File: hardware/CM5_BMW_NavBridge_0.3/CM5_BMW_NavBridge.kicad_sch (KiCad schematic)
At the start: 19 parts, among them CN1 10164227-1001A1RLF, CN2 10164227-1001A1RLF, CN3 X1313 Car connector, CN4 Molex to X1313 NAV connector, J1 Conn_01x04, SW1 SW_nRPIBOOT, SW2 SW_DIP_x02

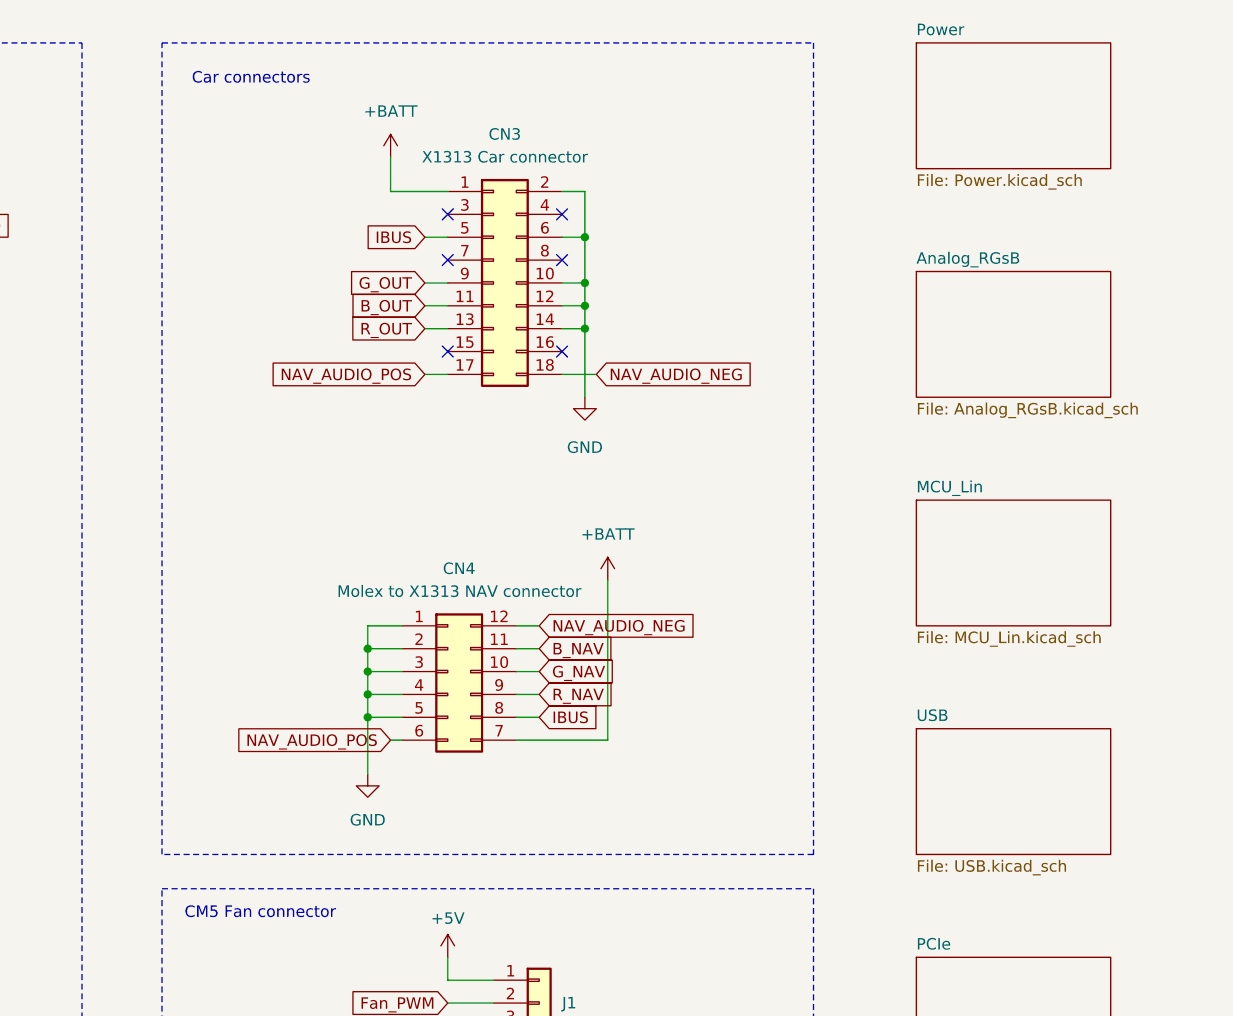
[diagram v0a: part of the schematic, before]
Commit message: finalized deletions and updated net deletes
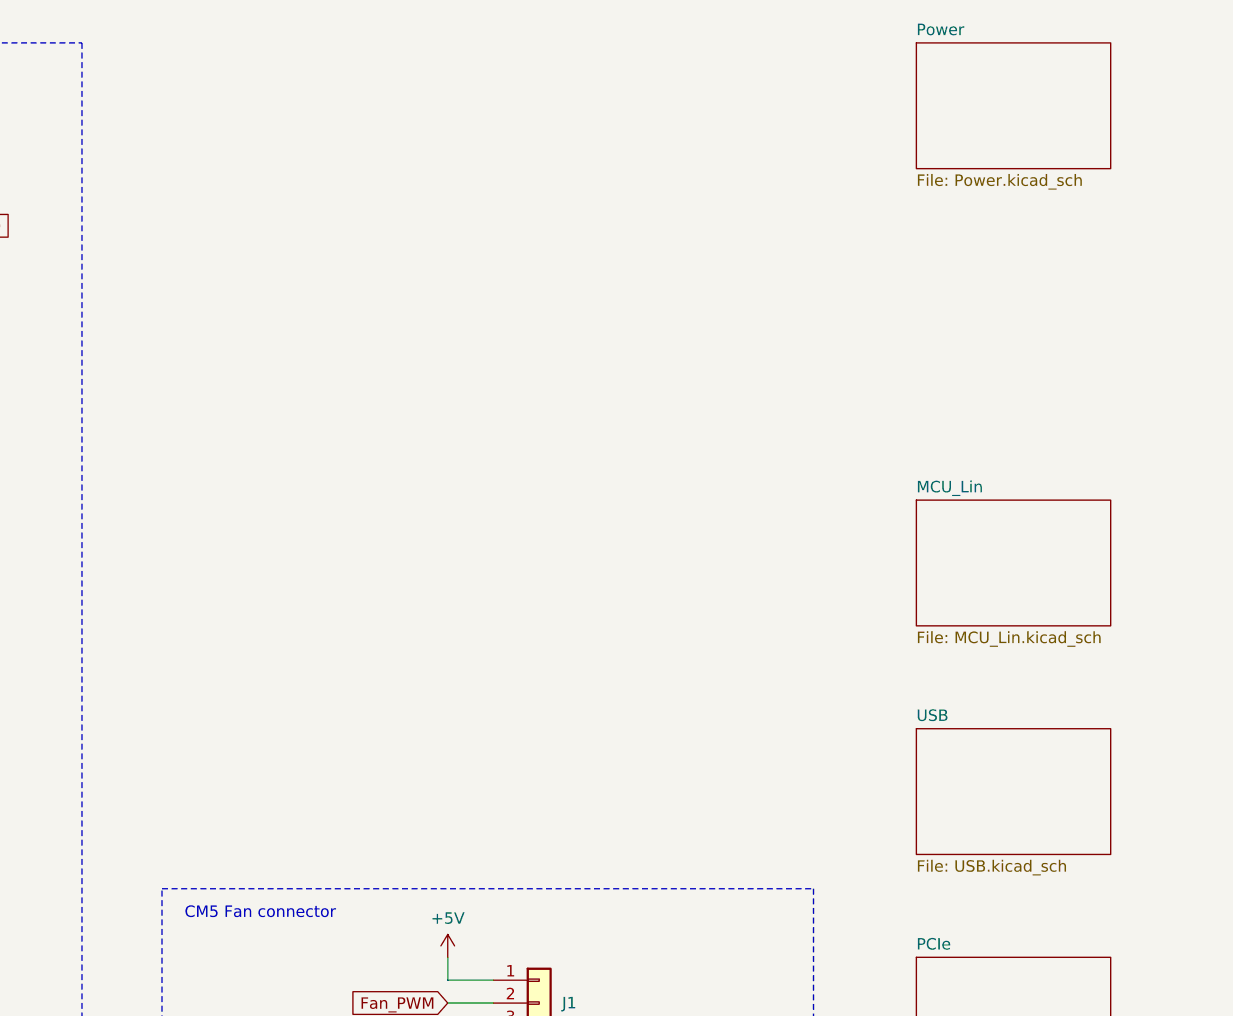
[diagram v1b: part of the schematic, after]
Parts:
- removed CN3: X1313 Car connector, Connector_PinHeader_2.54mm:PinHeader_2x09_P2.54mm_Horizontal, symbol Connector_Generic:Conn_02x09_Odd_Even
- removed CN4: Molex to X1313 NAV connector, Connector_Molex:Molex_Micro-Fit_3.0_43045-1200_2x06_P3.00mm_Horizontal, symbol Connector_Generic:Conn_02x06_Counter_Clockwise
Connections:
- no-connect marks 95 -> 89
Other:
- removed sheet Analog_RGsB
- note removed: "Car connectors"
